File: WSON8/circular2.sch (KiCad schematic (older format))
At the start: 34 parts, among them J101 Conn_Coaxial, J102 Conn_01x03, U101 LT3042xMSE, U102 LT3093xMSE, U103 OPA859xDSG

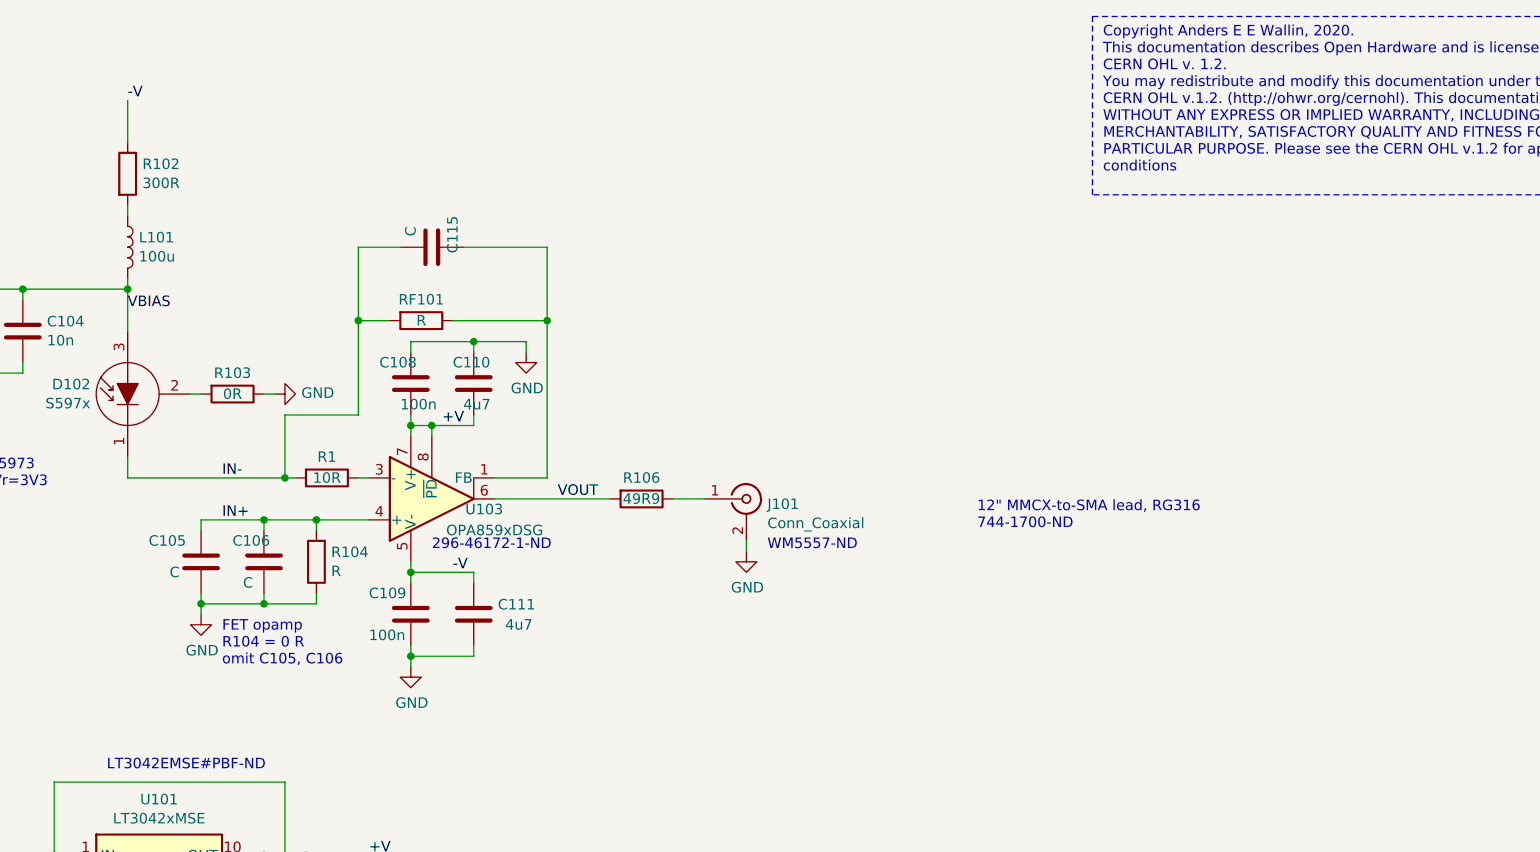
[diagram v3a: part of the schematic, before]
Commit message: add buffer to WSON8 design
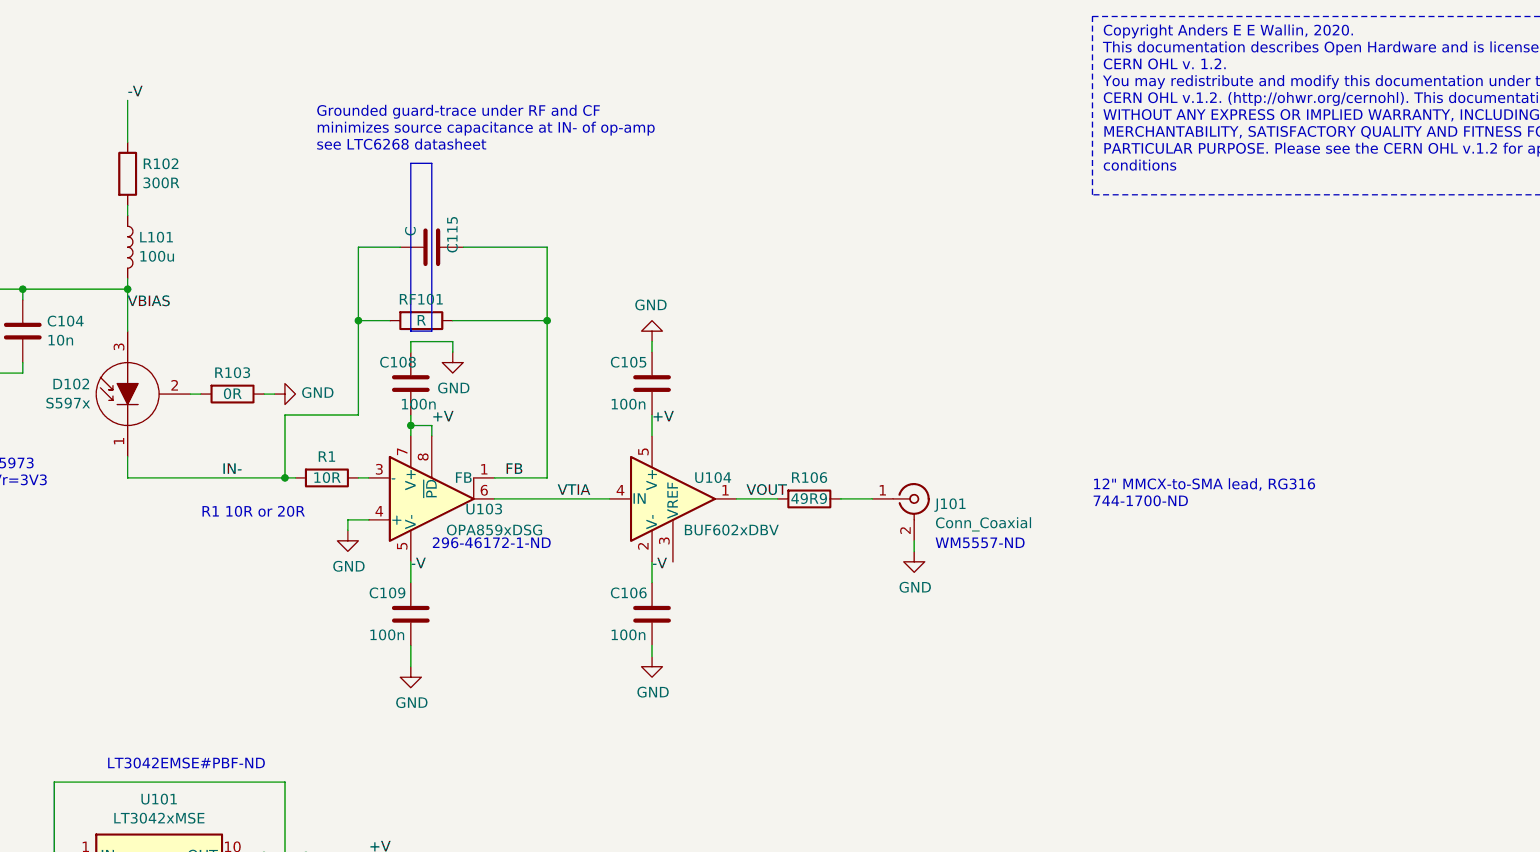
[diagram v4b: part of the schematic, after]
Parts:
- removed C110, C111: 4u7, Capacitor_SMD:C_0603_1608Metric, symbol Device:C
- removed R104: R, Resistor_SMD:R_0603_1608Metric, symbol Device:R
- added U104: BUF602xDBV, Package_TO_SOT_SMD:SOT-23-5, symbol Amplifier_Buffer:BUF602xDBV
- C105, C106: value C -> 100n
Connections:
- net +V: now also C105.2, U104.5 (V+)
- net -V: now also C106.1, U104.2 (V-)
- net GND: now also C105.1, U103.4 (+); no longer C105.2
- net VOUT: now also U104.1; no longer U103.6
- net FB: now reaches C115.1, RF101.1, U103.1 (FB)
- removed net IN+: C105.1, C106.1, U103.4 (+)
- new net VTIA: U103.6, U104.4 (IN)
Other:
- note added: "Grounded guard-trace under RF and CF\nminimizes source capacitance at IN- of op-amp\nsee LTC6268 datasheet"
- note added: "R1 10R or 20R"
- note removed: "FET opamp\nR104 = 0 R\nomit C105, C106"
- moved on the sheet: J101, R106
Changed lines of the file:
@@
 encoding utf-8
 Sheet 1 1
-Title "1\" Photodiode Transimpedance Amplifier - WSON8"
-Date "2019-12-20"
+Title "1\" Photodiode Transimpedance Amplifier - WSON8 + Buffer"
+Date "2020-05-12"
 Rev "draft"
 Comp "anders.e.e.wallin \"at\" gmail.com"
@@
 L Device:R R106
 U 1 1 5E0831FD
-P 5700 3050
-F 0 "R106" V 5600 3050 50  0000 C CNN
-F 1 "49R9" V 5700 3050 50  0000 C CNN
-F 2 "Resistor_SMD:R_0603_1608Metric" V 5630 3050 50  0001 C CNN
-F 3 "~" H 5700 3050 50  0001 C CNN
-	1    5700 3050
+P 6500 3050
+F 0 "R106" V 6400 3050 50  0000 C CNN
+F 1 "49R9" V 6500 3050 50  0000 C CNN
+F 2 "Resistor_SMD:R_0603_1608Metric" V 6430 3050 50  0001 C CNN
+F 3 "~" H 6500 3050 50  0001 C CNN
+	1    6500 3050
 	0    1    1    0
 $EndComp
@@
 L Connector:Conn_Coaxial J101
 U 1 1 5E083832
-P 6200 3050
-F 0 "J101" H 6300 3025 50  0000 L CNN
-F 1 "Conn_Coaxial" H 6300 2934 50  0000 L CNN
-F 2 "Connector_Coaxial:MMCX_Molex_73415-1471_Vertical" H 6200 3050 50  0001 C CNN
-F 3 " ~" H 6200 3050 50  0001 C CNN
-	1    6200 3050
-	1    0    0    -1
-$EndComp
-Wire Wire Line
-	6000 3050 5850 3050
+P 7000 3050
+F 0 "J101" H 7100 3025 50  0000 L CNN
+F 1 "Conn_Coaxial" H 7100 2934 50  0000 L CNN
+F 2 "Connector_Coaxial:MMCX_Molex_73415-1471_Vertical" H 7000 3050 50  0001 C CNN
+F 3 " ~" H 7000 3050 50  0001 C CNN
+	1    7000 3050
+	1    0    0    -1
+$EndComp
+Wire Wire Line
+	6800 3050 6650 3050
 $Comp
 L power:GND #PWR0102
 U 1 1 5E083EA7
-P 6200 3300
-F 0 "#PWR0102" H 6200 3050 50  0001 C CNN
-F 1 "GND" H 6205 3127 50  0000 C CNN
-F 2 "" H 6200 3300 50  0001 C CNN
-F 3 "" H 6200 3300 50  0001 C CNN
-	1    6200 3300
-	1    0    0    -1
-$EndComp
-Wire Wire Line
-	6200 3300 6200 3250
+P 7000 3300
+F 0 "#PWR0102" H 7000 3050 50  0001 C CNN
+F 1 "GND" H 7005 3127 50  0000 C CNN
+F 2 "" H 7000 3300 50  0001 C CNN
+F 3 "" H 7000 3300 50  0001 C CNN
+	1    7000 3300
+	1    0    0    -1
+$EndComp
+Wire Wire Line
+	7000 3300 7000 3250
 Wire Wire Line
 	3950 2550 3900 2550
 Wire Wire Line
 	3600 2550 3550 2550
-$Comp
-L Device:R R104
-U 1 1 5E0847DF
-P 4150 3350
-F 0 "R104" H 4080 3304 50  0000 R CNN
-F 1 "R" H 4080 3395 50  0000 R CNN
-F 2 "Resistor_SMD:R_0603_1608Metric" V 4080 3350 50  0001 C CNN
-F 3 "~" H 4150 3350 50  0001 C CNN
-	1    4150 3350
-	-1   0    0    1
-$EndComp
-Wire Wire Line
-	4400 3150 4150 3150
-Wire Wire Line
-	4150 3150 4150 3200
-$Comp
-L Device:C C106
-U 1 1 5E084F51
-P 3900 3350
-F 0 "C106" H 3750 3450 50  0000 L CNN
-F 1 "C" H 3800 3250 50  0000 L CNN
-F 2 "Capacitor_SMD:C_0603_1608Metric" H 3938 3200 50  0001 C CNN
-F 3 "~" H 3900 3350 50  0001 C CNN
-	1    3900 3350
-	1    0    0    -1
-$EndComp
-$Comp
-L Device:C C105
-U 1 1 5E0851CA
-P 3600 3350
-F 0 "C105" H 3350 3450 50  0000 L CNN
-F 1 "C" H 3450 3300 50  0000 L CNN
-F 2 "Capacitor_SMD:C_0603_1608Metric" H 3638 3200 50  0001 C CNN
-F 3 "~" H 3600 3350 50  0001 C CNN
-	1    3600 3350
-	1    0    0    -1
-$EndComp
 $Comp
 L power:GND #PWR0103
 U 1 1 5E0854FC
-P 3600 3600
-F 0 "#PWR0103" H 3600 3350 50  0001 C CNN
-F 1 "GND" H 3605 3427 50  0000 C CNN
-F 2 "" H 3600 3600 50  0001 C CNN
-F 3 "" H 3600 3600 50  0001 C CNN
-	1    3600 3600
-	1    0    0    -1
-$EndComp
-Wire Wire Line
-	3600 3600 3600 3550
-Wire Wire Line
-	3900 3500 3900 3550
-Wire Wire Line
-	3900 3550 3600 3550
-Connection ~ 3600 3550
-Wire Wire Line
-	3600 3550 3600 3500
-Wire Wire Line
-	4150 3500 4150 3550
-Wire Wire Line
-	4150 3550 3900 3550
-Connection ~ 3900 3550
-Wire Wire Line
-	4150 3150 3900 3150
-Wire Wire Line
-	3900 3150 3900 3200
-Connection ~ 4150 3150
-Wire Wire Line
-	3900 3150 3600 3150
-Wire Wire Line
-	3600 3150 3600 3200
-Connection ~ 3900 3150
+P 4300 3200
+F 0 "#PWR0103" H 4300 2950 50  0001 C CNN
+F 1 "GND" H 4305 3027 50  0000 C CNN
+F 2 "" H 4300 3200 50  0001 C CNN
+F 3 "" H 4300 3200 50  0001 C CNN
+	1    4300 3200
+	1    0    0    -1
+$EndComp
 $Comp
 L Device:C C109
@@
 $EndComp
 $Comp
-L Device:C C111
-U 1 1 5E08703F
-P 4900 3600
-F 0 "C111" H 5015 3646 50  0000 L CNN
-F 1 "4u7" H 5050 3550 50  0000 L CNN
-F 2 "Capacitor_SMD:C_0603_1608Metric" H 4938 3450 50  0001 C CNN
-F 3 "~" H 4900 3600 50  0001 C CNN
-	1    4900 3600
-	1    0    0    -1
-$EndComp
-$Comp
 L Device:C C108
 U 1 1 5E0879D1
@@
 	1    0    0    -1
 $EndComp
-$Comp
-L Device:C C110
-U 1 1 5E087CFB
-P 4900 2500
-F 0 "C110" H 4800 2600 50  0000 L CNN
-F 1 "4u7" H 4850 2400 50  0000 L CNN
-F 2 "Capacitor_SMD:C_0603_1608Metric" H 4938 2350 50  0001 C CNN
-F 3 "~" H 4900 2500 50  0001 C CNN
-	1    4900 2500
-	1    0    0    -1
-$EndComp
 Wire Wire Line
 	4350 2200 4500 2200
@@
 Wire Wire Line
 	4600 2700 4700 2700
-Wire Wire Line
-	4900 2700 4900 2650
 Connection ~ 4600 2700
 Wire Wire Line
 	4600 2700 4600 2650
-Wire Wire Line
-	4600 3350 4600 3400
-Wire Wire Line
-	4600 3400 4900 3400
-Wire Wire Line
-	4900 3400 4900 3450
-Connection ~ 4600 3400
-Wire Wire Line
-	4600 3400 4600 3450
-Text Label 4750 2700 0    50   ~ 0
+Text Label 4700 2700 0    50   ~ 0
 +V
 $Comp
@@
 	1    0    0    -1
 $EndComp
-Wire Wire Line
-	4600 3850 4600 3800
-Wire Wire Line
-	4900 3750 4900 3800
-Wire Wire Line
-	4900 3800 4600 3800
-Connection ~ 4600 3800
-Wire Wire Line
-	4600 3800 4600 3750
 $Comp
 L power:GND #PWR0105
 U 1 1 5E08C63D
-P 5150 2350
-F 0 "#PWR0105" H 5150 2100 50  0001 C CNN
-F 1 "GND" H 5155 2177 50  0000 C CNN
-F 2 "" H 5150 2350 50  0001 C CNN
-F 3 "" H 5150 2350 50  0001 C CNN
-	1    5150 2350
-	1    0    0    -1
-$EndComp
-Wire Wire Line
-	5150 2350 5150 2300
-Wire Wire Line
-	5150 2300 4900 2300
+P 4800 2350
+F 0 "#PWR0105" H 4800 2100 50  0001 C CNN
+F 1 "GND" H 4805 2177 50  0000 C CNN
+F 2 "" H 4800 2350 50  0001 C CNN
+F 3 "" H 4800 2350 50  0001 C CNN
+	1    4800 2350
+	1    0    0    -1
+$EndComp
 Wire Wire Line
 	4600 2300 4600 2350
-Wire Wire Line
-	4900 2350 4900 2300
-Connection ~ 4900 2300
-Wire Wire Line
-	4900 2300 4600 2300
-Text Label 4800 3400 0    50   ~ 0
+Text Label 4600 3400 0    50   ~ 0
 -V
 $Comp
@@
 Text Notes 3050 7200 0    50   ~ 0
 LT3093EMSE#PBF-ND
-Text Notes 6300 3300 0    50   ~ 0
+Text Notes 7100 3300 0    50   ~ 0
 WM5557-ND
-Text Notes 7300 3200 0    50   ~ 0
+Text Notes 7850 3100 0    50   ~ 0
 12" MMCX-to-SMA lead, RG316\n744-1700-ND
 Text Label 1650 6100 0    50   ~ 0
@@
 VBIAS
 Text Label 5300 3050 0    50   ~ 0
-VOUT
+VTIA
 $Comp
 L Device:C C115
@@
 Wire Wire Line
 	4700 2750 4700 2700
-Connection ~ 4700 2700
-Wire Wire Line
-	4700 2700 4900 2700
-Text Label 3700 3150 0    50   ~ 0
-IN+
 Text Label 3700 2950 0    50   ~ 0
 IN-
@@
 Wire Notes Line
 	7850 1600 7850 750
-Text Notes 3700 3850 0    50   ~ 0
-FET opamp\nR104 = 0 R\nomit C105, C106
+Wire Wire Line
+	4400 3150 4300 3150
+Wire Wire Line
+	4300 3150 4300 3200
+$Comp
+L Amplifier_Buffer:BUF602xDBV U104
+U 1 1 5EBC4501
+P 5850 3050
+F 0 "U104" H 5950 3150 50  0000 L CNN
+F 1 "BUF602xDBV" H 5900 2900 50  0000 L CNN
+F 2 "Package_TO_SOT_SMD:SOT-23-5" H 5850 2750 50  0001 C CNN
+F 3 "http://www.ti.com/lit/ds/symlink/buf602.pdf" H 5850 3050 50  0001 C CNN
+	1    5850 3050
+	1    0    0    -1
+$EndComp
+Wire Wire Line
+	6350 3050 6150 3050
+Wire Wire Line
+	4600 3350 4600 3450
+Wire Wire Line
+	4600 3750 4600 3850
+$Comp
+L Device:C C106
+U 1 1 5EBD2426
+P 5750 3600
+F 0 "C106" H 5550 3700 50  0000 L CNN
+F 1 "100n" H 5550 3500 50  0000 L CNN
+F 2 "Capacitor_SMD:C_0603_1608Metric" H 5788 3450 50  0001 C CNN
+F 3 "~" H 5750 3600 50  0001 C CNN
+	1    5750 3600
+	1    0    0    -1
+$EndComp
+$Comp
+L power:GND #PWR0118
+U 1 1 5EBD2E5E
+P 5750 3800
+F 0 "#PWR0118" H 5750 3550 50  0001 C CNN
+F 1 "GND" H 5755 3627 50  0000 C CNN
+F 2 "" H 5750 3800 50  0001 C CNN
+F 3 "" H 5750 3800 50  0001 C CNN
+	1    5750 3800
+	1    0    0    -1
+$EndComp
+Wire Wire Line
+	5750 3800 5750 3750
+Text Label 5750 3400 0    50   ~ 0
+-V
+Wire Wire Line
+	5750 3350 5750 3450
+$Comp
+L Device:C C105
+U 1 1 5EBD9F0A
+P 5750 2500
+F 0 "C105" H 5550 2600 50  0000 L CNN
+F 1 "100n" H 5550 2400 50  0000 L CNN
+F 2 "Capacitor_SMD:C_0603_1608Metric" H 5788 2350 50  0001 C CNN
+F 3 "~" H 5750 2500 50  0001 C CNN
+	1    5750 2500
+	1    0    0    -1
+$EndComp
+Text Label 5750 2700 0    50   ~ 0
++V
+Wire Wire Line
+	5750 2650 5750 2750
+$Comp
+L power:GND #PWR0119
+U 1 1 5EBDE11C
+P 5750 2300
+F 0 "#PWR0119" H 5750 2050 50  0001 C CNN
+F 1 "GND" H 5755 2127 50  0000 C CNN
+F 2 "" H 5750 2300 50  0001 C CNN
+F 3 "" H 5750 2300 50  0001 C CNN
+	1    5750 2300
+	-1   0    0    1
+$EndComp
+Wire Wire Line
+	5750 2350 5750 2300
+Text Label 6200 3050 0    50   ~ 0
+VOUT
+Text Label 5050 2950 0    50   ~ 0
+FB
+Wire Wire Line
+	4800 2350 4800 2300
+Wire Wire Line
+	4800 2300 4600 2300
+Wire Bus Line
+	4600 1450 4600 2250
+Wire Bus Line
+	4600 2250 4700 2250
+Wire Bus Line
+	4700 2250 4700 1450
+Wire Bus Line
+	4700 1450 4600 1450
+Text Notes 4150 1400 0    50   ~ 0
+Grounded guard-trace under RF and CF\nminimizes source capacitance at IN- of op-amp\nsee LTC6268 datasheet
+Text Notes 3600 3150 0    50   ~ 0
+R1 10R or 20R
 $EndSCHEMATC
